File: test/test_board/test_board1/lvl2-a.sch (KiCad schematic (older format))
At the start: 1 part, among them U9 MMA865x

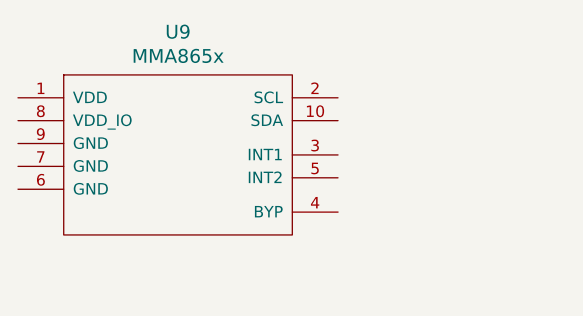
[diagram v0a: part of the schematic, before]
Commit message: Adding some test boards
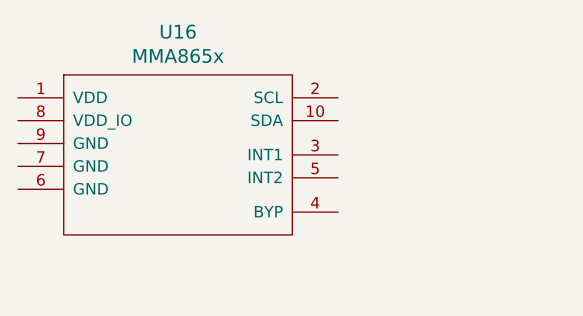
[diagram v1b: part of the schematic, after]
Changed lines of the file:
@@
 $Descr A4 11693 8268
 encoding utf-8
-Sheet 3 7
+Sheet 3 11
 Title ""
 Date ""
@@
 $Comp
 L accelerometer:MMA865x U9
-U 1 1 5E67F437
+U 1 1 5E6EC240
 P 4500 2950
-AR Path="/5E6781CF/5E67F299/5E67F437" Ref="U9" Part="1"
-AR Path="/5E678707/5E67F299/5E67F437" Ref="U10" Part="1"
-F 0 "U9" H 4500 3687 60 0000 C CNN
+AR Path="/5E6781CF/5E67F299/5E6EC240" Ref="U9" Part="1"
+AR Path="/5E678707/5E67F299/5E6EC240" Ref="U10" Part="1"
+AR Path="/5E6EC0CC/5E67F299/5E6EC240" Ref="U16" Part="1"
+F 0 "U16" H 4500 3687 60 0000 C CNN
 F 1 "MMA865x" H 4500 3581 60 0000 C CNN
 F 2 "" H 4350 3150 60 0001 C CNN

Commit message: Adding schematic editor to associate kicad parts with kipartman parts
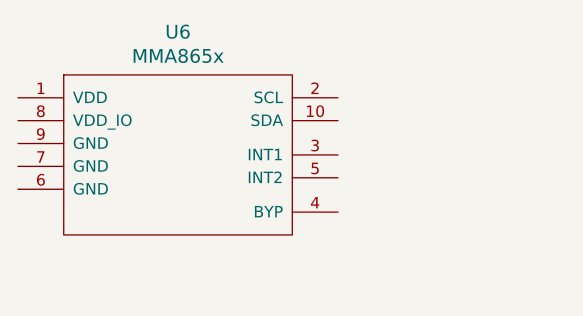
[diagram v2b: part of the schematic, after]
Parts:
- renumbered U9 to U6
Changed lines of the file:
@@
 $EndDescr
 $Comp
-L accelerometer:MMA865x U9
+L accelerometer:MMA865x U6
 U 1 1 5E6EC240
 P 4500 2950
-AR Path="/5E6781CF/5E67F299/5E6EC240" Ref="U9" Part="1"
-AR Path="/5E678707/5E67F299/5E6EC240" Ref="U10" Part="1"
-AR Path="/5E6EC0CC/5E67F299/5E6EC240" Ref="U16" Part="1"
-F 0 "U16" H 4500 3687 60 0000 C CNN
-F 1 "MMA865x" H 4500 3581 60 0000 C CNN
-F 2 "" H 4350 3150 60 0001 C CNN
-F 3 "" H 4350 3150 60 0001 C CNN
-F 4 "139" H 0 0 0 0001 C CNN "kipart_id"
-F 5 "MMA845x" H 0 0 0 0001 C CNN "kipart_sku"
-1 4500 2950
-1 0 0 -1
+AR Path="/5E6781CF/5E67F299/5E6EC240" Ref="U6"  Part="1"
+AR Path="/5E678707/5E67F299/5E6EC240" Ref="U11"  Part="1"
+AR Path="/5E6EC0CC/5E67F299/5E6EC240" Ref="U16"  Part="1"
+AR Path="/5E6EC240" Ref="U?"  Part="1"
+F 0 "U6" H 4500 3687 60  0000 C CNN
+F 1 "MMA865x" H 4500 3581 60  0000 C CNN
+F 2 "" H 4350 3150 60  0001 C CNN
+F 3 "" H 4350 3150 60  0001 C CNN
+F 4 "139" H 0   0   0   0001 C CNN "kipart_id"
+F 5 "MMA845x" H 0   0   0   0001 C CNN "kipart_sku"
+	1    4500 2950
+	1    0    0    -1
 $EndComp
 $Sheet
